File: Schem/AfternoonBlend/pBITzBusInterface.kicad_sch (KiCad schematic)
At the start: 1 part, among them J1 pBITzBus

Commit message: Added a buffer on the Data Line to avoid overloading the CPU data bus with the 5 ICs on the board.
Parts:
- added C20: 100n, Capacitor_SMD:C_0603_1608Metric, symbol Device:C
- added U4: 74HCT541, Package_SO:TSSOP-20-1EP_4.4x6.5mm_P0.65mm_EP2.15x3.35mm, symbol 74xx:74HCT541
- J1: MANUFACTURER_PART_NUMBER (none) -> 74HCT541PW,118
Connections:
- net +5V: now also C20.1, U4.20 (VCC)
- net D0: now also U4.2 (A0)
- net D1: now also U4.3 (A1)
- net D2: now also U4.4 (A2)
- net D3: now also U4.5 (A3)
- net D4: now also U4.6 (A4)
- net D5: now also U4.7 (A5)
- net D6: now also U4.8 (A6)
- net D7: now also U4.9 (A7)
- net GND: now also C20.2, U4.1 (G1), U4.10 (GND), U4.19 (G2)
- new net DB0: U4.18 (Y0)
- new net DB1: U4.17 (Y1)
- new net DB2: U4.16 (Y2)
- new net DB3: U4.15 (Y3)
- new net DB4: U4.14 (Y4)
- new net DB5: U4.13 (Y5)
- new net DB6: U4.12 (Y6)
- new net DB7: U4.11 (Y7)
- no-connect marks 66 -> 65

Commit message: Added wait-state generation to cope with a 10MHz cpu
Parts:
- J1: MANUFACTURER_PART_NUMBER 74HCT541PW,118 -> (none)
- U4: footprint Package_SO:TSSOP-20-1EP_4.4x6.5mm_P0.65mm_EP2.15x3.35mm -> Package_SO:TSSOP-20_4.4x6.5mm_P0.65mm; MANUFACTURER_PART_NUMBER (none) -> 74HCT541PW,118
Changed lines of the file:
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@@
 			)
 		)
-		(property "Footprint" "Package_SO:TSSOP-20-1EP_4.4x6.5mm_P0.65mm_EP2.15x3.35mm"
+		(property "Footprint" "Package_SO:TSSOP-20_4.4x6.5mm_P0.65mm"
 			(at 187.96 177.8 0)
 			(hide yes)
@@
 		)
 		(property "Description" "8-bit Buffer/Line Driver 3-state outputs"
+			(at 187.96 177.8 0)
+			(hide yes)
+			(show_name no)
+			(do_not_autoplace no)
+			(effects
+				(font
+					(size 1.27 1.27)
+				)
+			)
+		)
+		(property "MANUFACTURER_PART_NUMBER" "74HCT541PW,118"
 			(at 187.96 177.8 0)
 			(hide yes)
@@
 			)
 		)
-		(property "MANUFACTURER_PART_NUMBER" "74HCT541PW,118"
+		(property "MANUFACTURER_PART_NUMBER" ""
 			(at 251.46 180.34 0)
 			(hide yes)
@@
 			)
 		)
-		(property "MANUFACTURER_PART_NUMBER" "74HCT541PW,118"
+		(property "MANUFACTURER_PART_NUMBER" ""
 			(at 251.46 217.17 0)
 			(hide yes)
@@
 			)
 		)
-		(property "MANUFACTURER_PART_NUMBER" "74HCT541PW,118"
+		(property "MANUFACTURER_PART_NUMBER" ""
 			(at 120.65 166.37 0)
 			(hide yes)

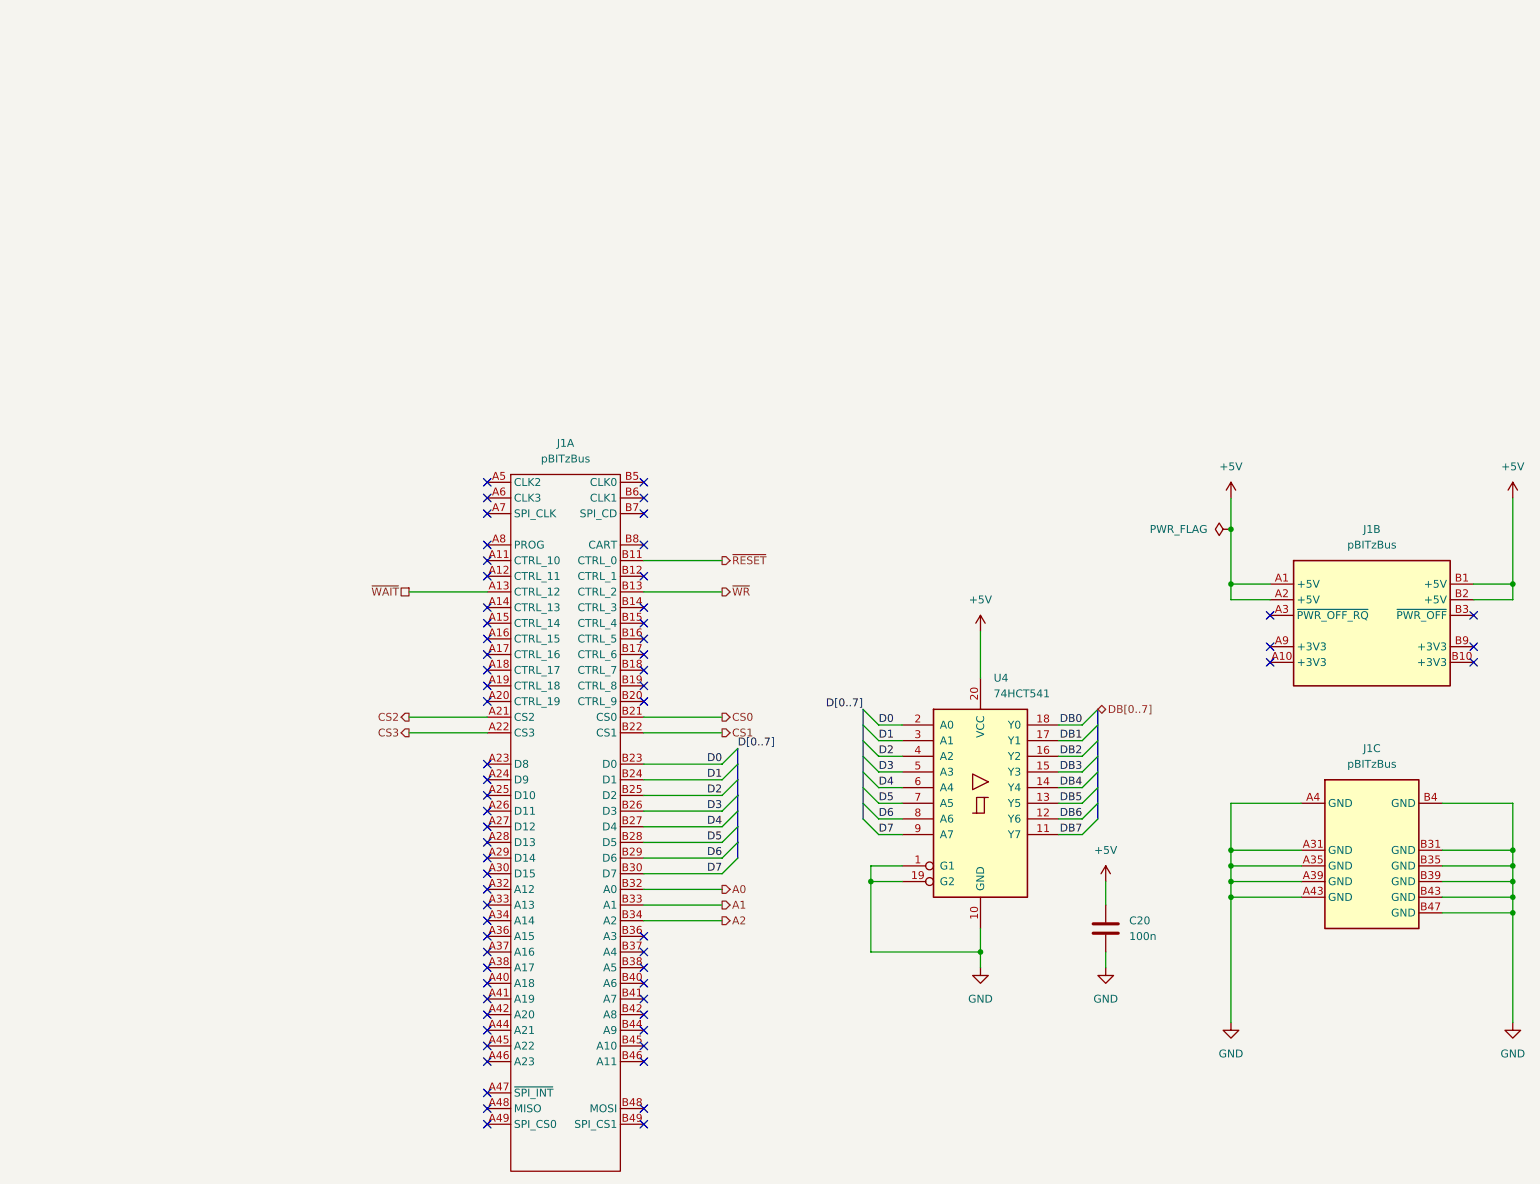
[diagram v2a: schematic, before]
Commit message: Moved to the DIN Connector
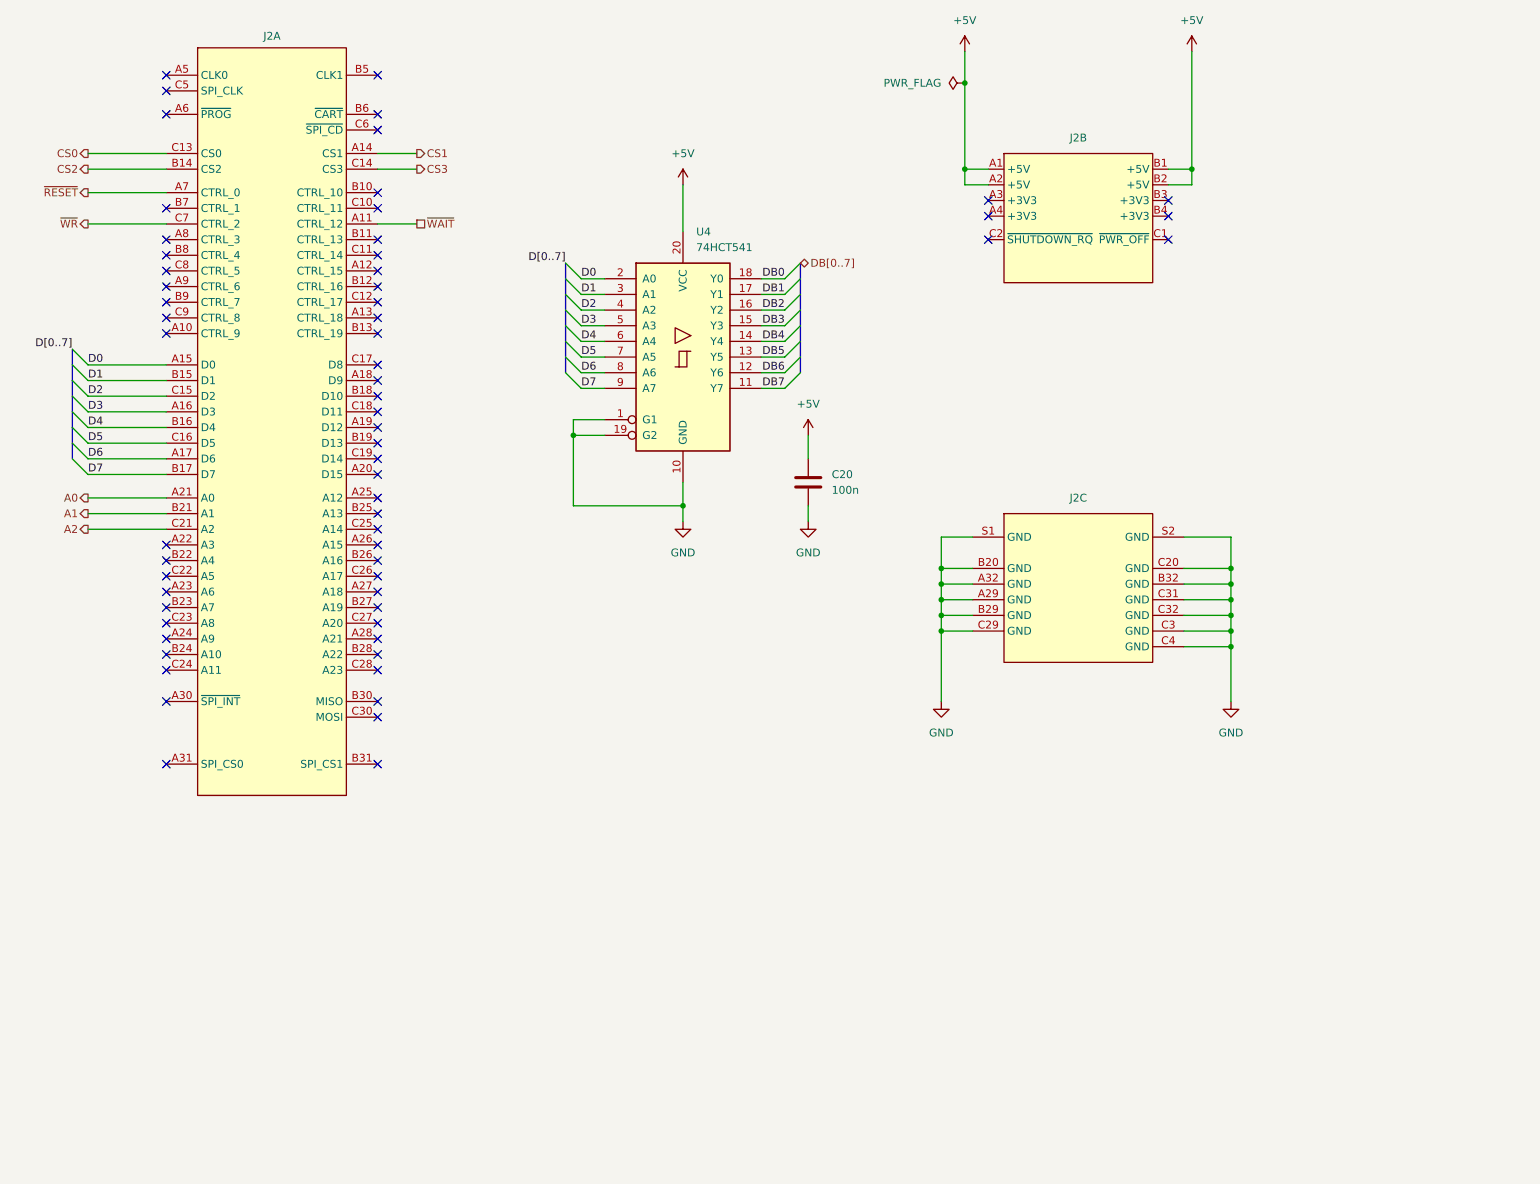
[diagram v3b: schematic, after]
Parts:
- removed J1: pBITzBus, Connector_PCBEdge:BUS_PCIexpress_x8, symbol pBITz:pBITzBus
- added J2: (no value), Footprints:AMPHENOL_86093967113T55F1LF, symbol pBITz:pBITzBus_DIN
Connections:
- net +5V: now also J2.A1 (+5V), J2.A2 (+5V), J2.B1 (+5V), J2.B2 (+5V)
- net A0: now also J2.A21 (A0)
- net A1: now also J2.B21 (A1)
- net A2: now also J2.C21 (A2)
- net CS0: now also J2.C13 (CS0)
- net CS1: now also J2.A14 (CS1)
- net CS2: now also J2.B14 (CS2)
- net CS3: now also J2.C14 (CS3)
- net D0: now also J2.A15 (D0)
- net D1: now also J2.B15 (D1)
- net D2: now also J2.C15 (D2)
- net D3: now also J2.A16 (D3)
- net D4: now also J2.B16 (D4)
- net D5: now also J2.C16 (D5)
- net D6: now also J2.A17 (D6)
- net D7: now also J2.B17 (D7)
- net GND: now also J2.A29 (GND), J2.A32 (GND), J2.B20 (GND), J2.B29 (GND), J2.B32 (GND), J2.C20 (GND), J2.C29 (GND), J2.C3 (GND), J2.C31 (GND), J2.C32 (GND), J2.C4 (GND), J2.S1 (GND), J2.S2 (GND)
- net ~{RESET}: now also J2.A7 (CTRL_0)
- net ~{WAIT}: now also J2.A11 (CTRL_12)
- net ~{WR}: now also J2.C7 (CTRL_2)
- no-connect marks 65 -> 63
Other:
- moved on the sheet: C20, U4

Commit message: updated the part #s
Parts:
- J2: MANUFACTURER_PART_NUMBER (none) -> 86093967113T55F1LF
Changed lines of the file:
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@@
+			)
+		)
+		(property "MANUFACTURER_PART_NUMBER" "86093967113T55F1LF"
+			(at 203.835 128.27 0)
+			(hide yes)
+			(show_name no)
+			(do_not_autoplace no)
+			(effects
+				(font
+					(size 1.27 1.27)
+				)
 			)
 		)
@@
 			)
 		)
+		(property "MANUFACTURER_PART_NUMBER" "86093967113T55F1LF"
+			(at 203.835 71.12 0)
+			(hide yes)
+			(show_name no)
+			(do_not_autoplace no)
+			(effects
+				(font
+					(size 1.27 1.27)
+				)
+			)
+		)
 		(pin "B13"
 		)
@@
 			(at 73.025 53.34 0)
 			(hide yes)
+			(show_name no)
+			(do_not_autoplace no)
+			(effects
+				(font
+					(size 1.27 1.27)
+				)
+			)
+		)
+		(property "MANUFACTURER_PART_NUMBER" "86093967113T55F1LF"
+			(at 73.025 53.34 0)
+			(hide yes)
